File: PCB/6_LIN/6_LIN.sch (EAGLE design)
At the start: 8 parts, among them IC6 MCP2003, X12 ALLSERIALD, X6 AKL18X-03W

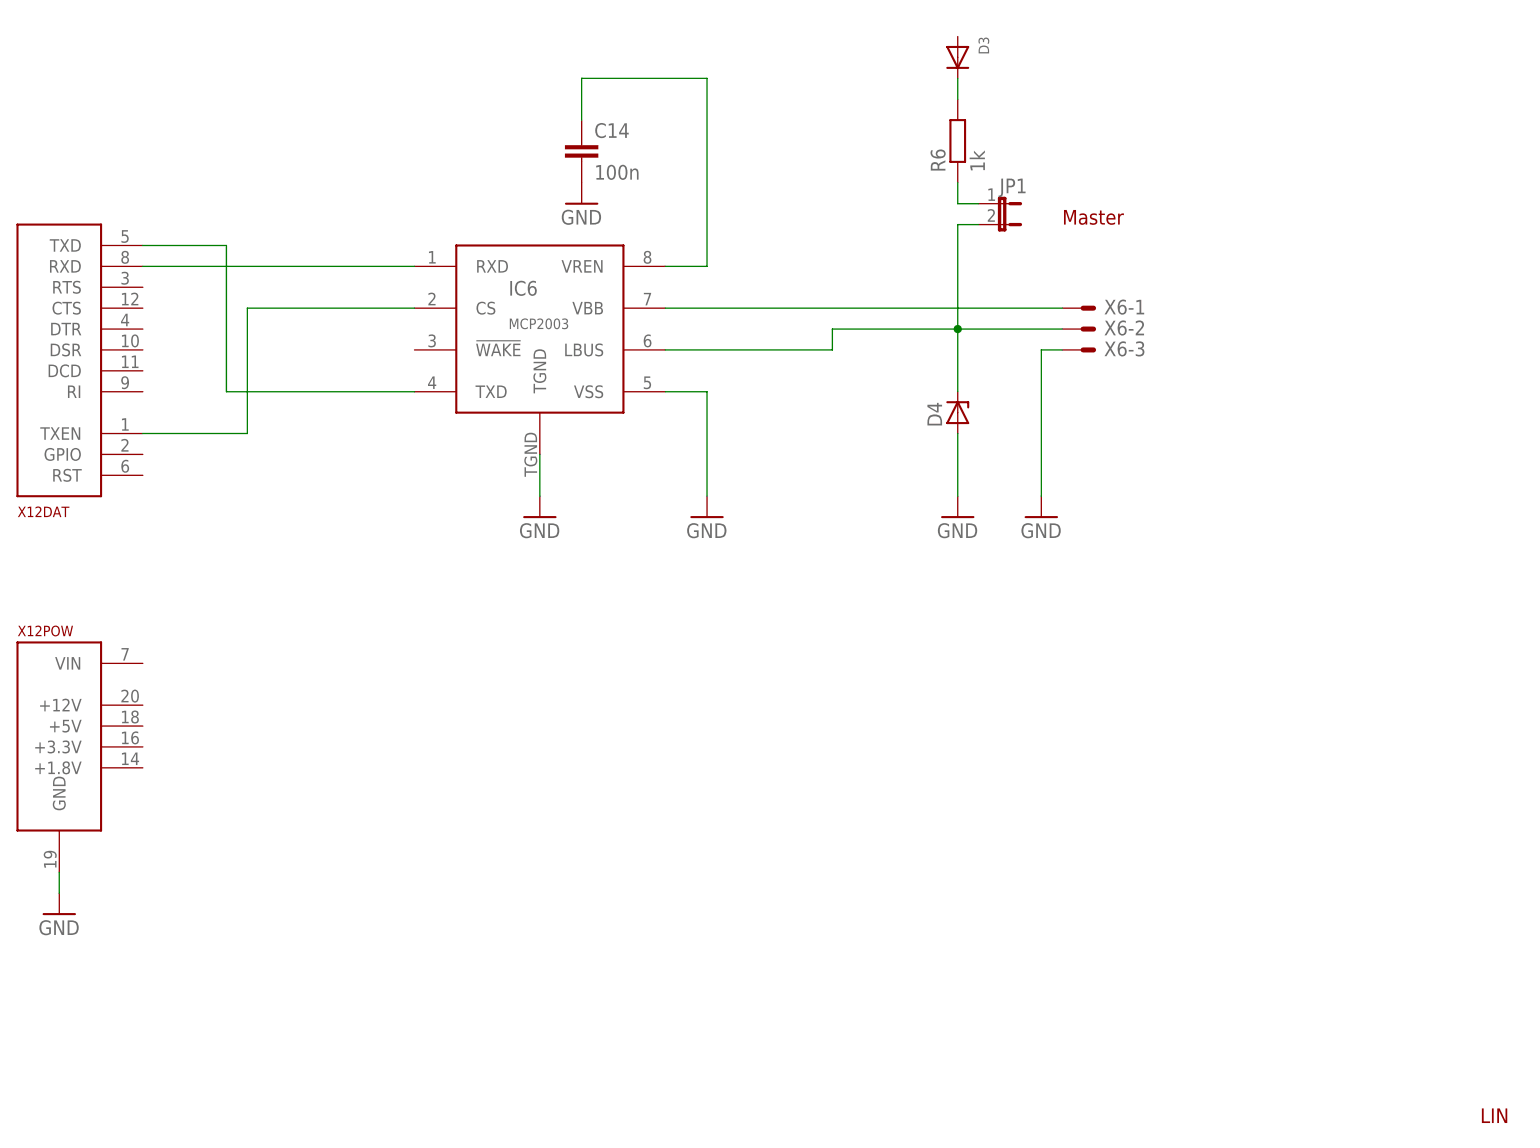
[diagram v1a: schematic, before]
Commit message: finish LIN schematic
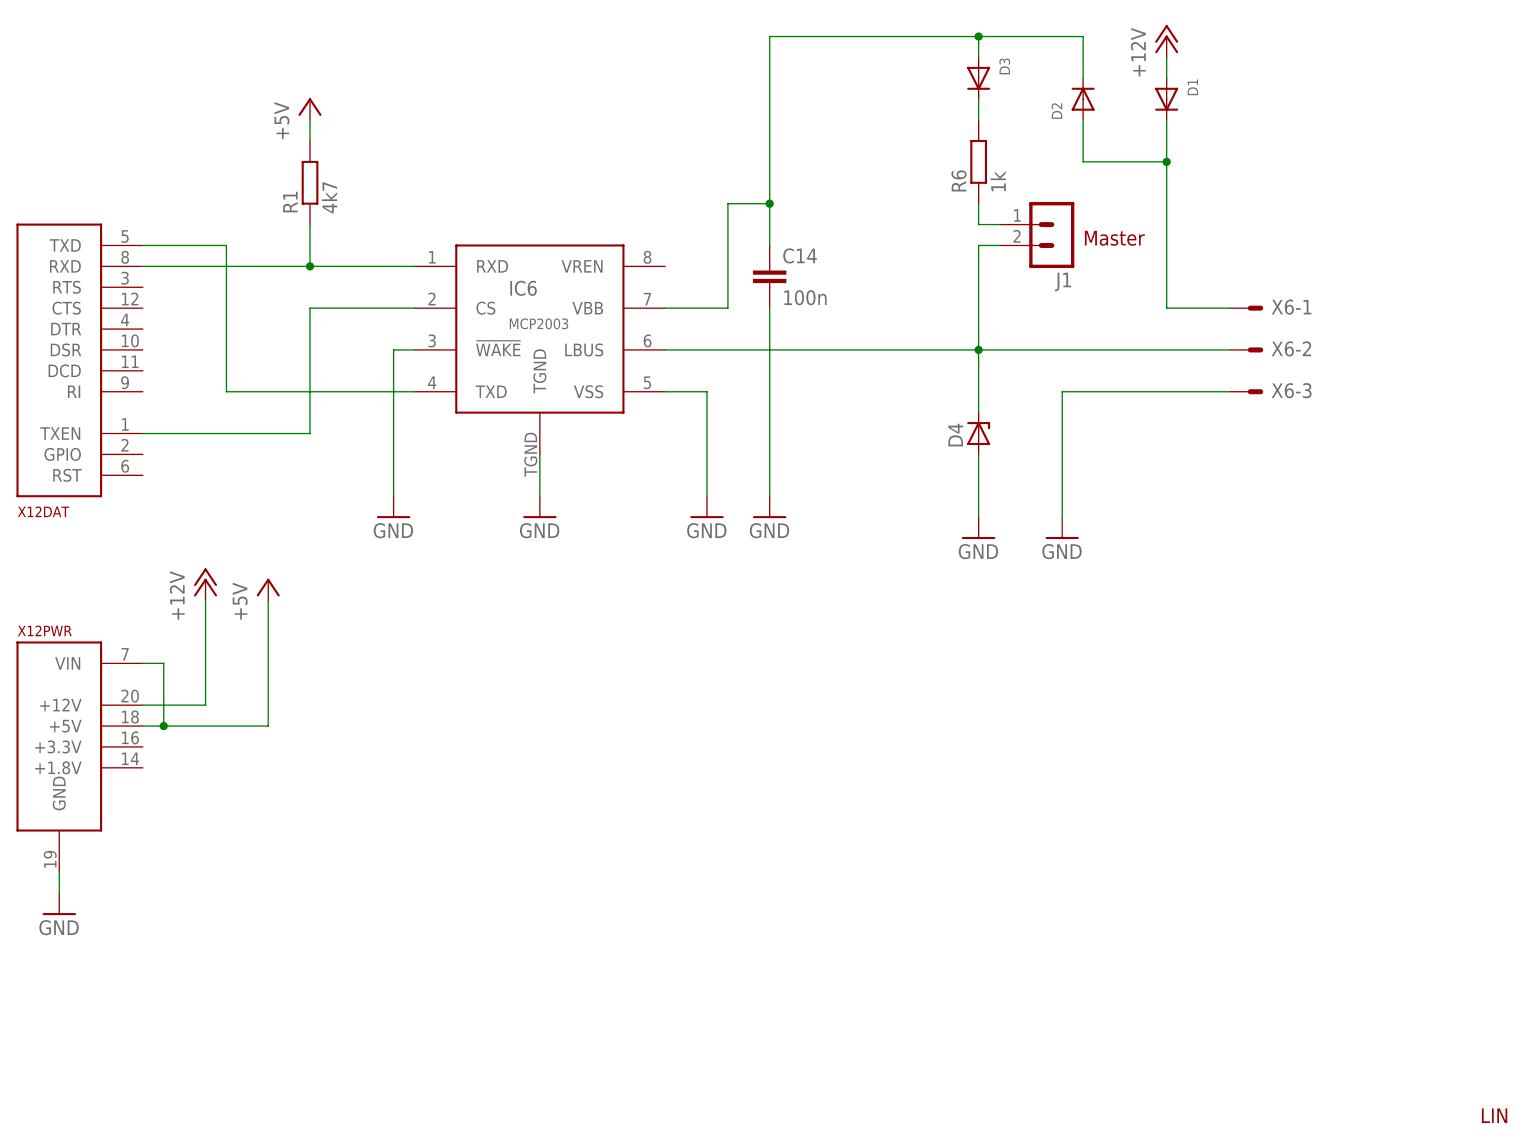
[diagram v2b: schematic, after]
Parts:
- removed JP1: (no value), jumper:JP1E
- added D1, D2: (no value), microbuilder:DIODESOD-123
- added J1: MA02-1W, con-lstb:MA02-1W
- added R1: 4k7, rcl:R-EU_R0805
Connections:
- removed net N$72: IC6.VBB, X6-1.S
- removed net N$76: C14.1, IC6.VREN
- new net +12V: D1.A, X12PWR.+12V
- new net +5V: R1.2, X12PWR.+5V, X12PWR.VIN
- new net N$1: D1.C, D2.A, X6-1.S
- new net N$2: C14.1, D2.C, D3.A, IC6.VBB
- net GND: now also IC6.!WAKE, X12PWR.GND; no longer X12POW.GND
- net N$73: now also J1.2; no longer JP1.2
- net N$74: now also J1.1; no longer JP1.1
- net N$79: now also R1.1
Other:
- moved on the sheet: C14, D3, D4, R6, X6-1, X6-2, X6-3
